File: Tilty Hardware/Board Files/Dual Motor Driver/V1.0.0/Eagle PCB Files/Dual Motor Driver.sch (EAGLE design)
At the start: 43 parts, among them J1 AVR_SPI_PRG_62X3_LOCK, Q1 16MHz, U1 ATMEGA328P, U2 L298_BRIDGE_DRIVER, U3 LM2931

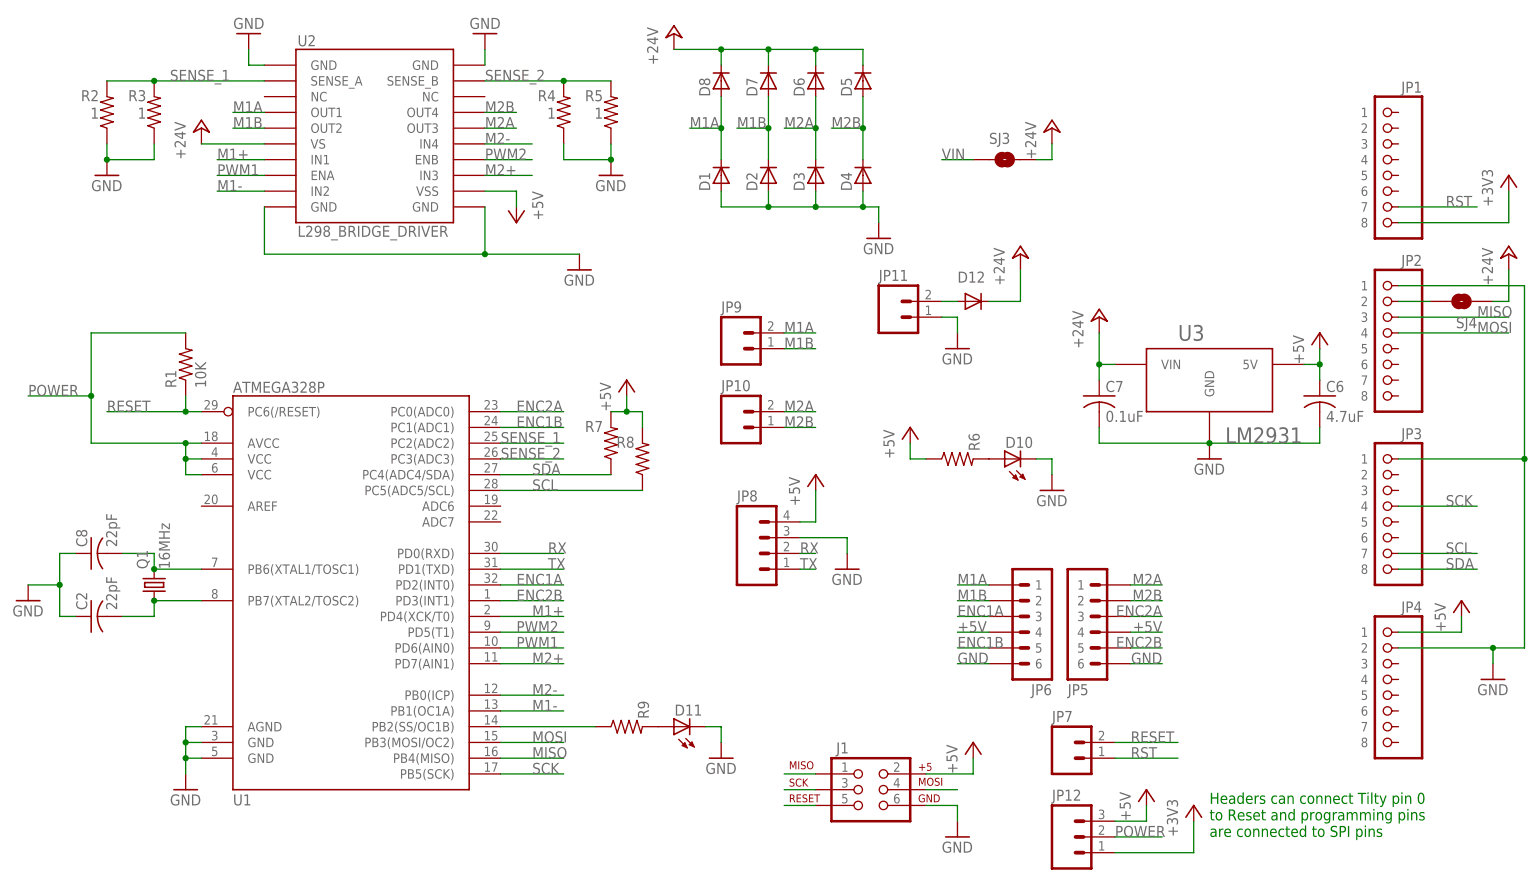
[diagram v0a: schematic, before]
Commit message: Updated some pin connection names on the Dual Motor Driver schematic
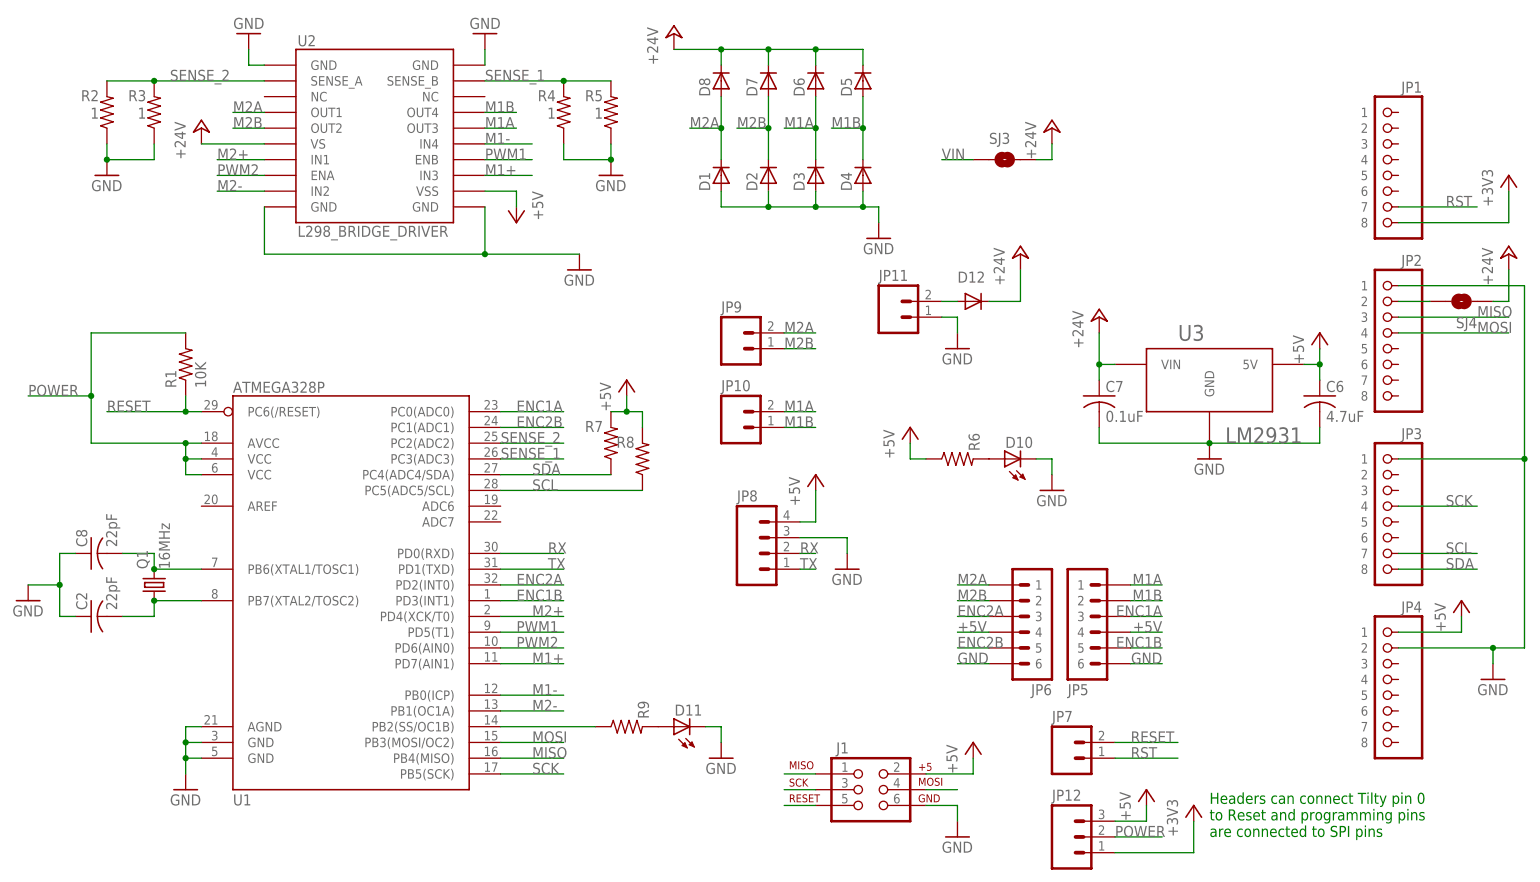
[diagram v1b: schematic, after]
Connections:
- net ENC1A: now also JP5.3, U1.PC0(ADC0); no longer JP6.3, U1.PD2(INT0)
- net ENC1B: now also JP5.5, U1.PD3(INT1); no longer JP6.5, U1.PC1(ADC1)
- net ENC2A: now also JP6.3, U1.PD2(INT0); no longer JP5.3, U1.PC0(ADC0)
- net ENC2B: now also JP6.5, U1.PC1(ADC1); no longer JP5.5, U1.PD3(INT1)
- net M1+: now also U1.PD7(AIN1), U2.IN3; no longer U1.PD4(XCK/T0), U2.IN1
- net M1-: now also U1.PB0(ICP), U2.IN4; no longer U1.PB1(OC1A), U2.IN2
- net M1A: now also D3.C, D6.A, JP10.2, JP5.1, U2.OUT3; no longer D1.C, D8.A, JP6.1, JP9.2, U2.OUT1
- net M1B: now also D4.C, D5.A, JP10.1, JP5.2, U2.OUT4; no longer D2.C, D7.A, JP6.2, JP9.1, U2.OUT2
- net M2+: now also U1.PD4(XCK/T0), U2.IN1; no longer U1.PD7(AIN1), U2.IN3
- net M2-: now also U1.PB1(OC1A), U2.IN2; no longer U1.PB0(ICP), U2.IN4
- net M2A: now also D1.C, D8.A, JP6.1, JP9.2, U2.OUT1; no longer D3.C, D6.A, JP10.2, JP5.1, U2.OUT3
- net M2B: now also D2.C, D7.A, JP6.2, JP9.1, U2.OUT2; no longer D4.C, D5.A, JP10.1, JP5.2, U2.OUT4
- net PWM1: now also U1.PD5(T1), U2.ENB; no longer U1.PD6(AIN0), U2.ENA
- net PWM2: now also U1.PD6(AIN0), U2.ENA; no longer U1.PD5(T1), U2.ENB
- net SENSE_1: now also R4.2, R5.2, U1.PC3(ADC3), U2.SENSE_B; no longer R2.2, R3.2, U1.PC2(ADC2), U2.SENSE_A
- net SENSE_2: now also R2.2, R3.2, U1.PC2(ADC2), U2.SENSE_A; no longer R4.2, R5.2, U1.PC3(ADC3), U2.SENSE_B
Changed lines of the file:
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@@
 </segment>
 </net>
-<net name="M1A" class="0">
+<net name="M2A" class="0">
 <segment>
 <pinref part="D1" gate="G$1" pin="C"/>
@@
 </segment>
 </net>
-<net name="M1B" class="0">
+<net name="M2B" class="0">
 <segment>
 <wire x1="116.84" y1="109.22" x2="116.84" y2="114.3" width="0.1524" layer="91"/>
@@
 </segment>
 </net>
-<net name="M2A" class="0">
+<net name="M1A" class="0">
 <segment>
 <wire x1="124.46" y1="109.22" x2="124.46" y2="114.3" width="0.1524" layer="91"/>
@@
 </segment>
 </net>
-<net name="M2B" class="0">
+<net name="M1B" class="0">
 <segment>
 <wire x1="132.08" y1="109.22" x2="132.08" y2="114.3" width="0.1524" layer="91"/>
@@
 </segment>
 </net>
-<net name="ENC1B" class="0">
+<net name="ENC2B" class="0">
 <segment>
 <pinref part="U1" gate="G$1" pin="PC1(ADC1)"/>
@@
 </segment>
 </net>
-<net name="ENC1A" class="0">
+<net name="ENC2A" class="0">
 <segment>
 <pinref part="JP6" gate="1" pin="3"/>
@@
 </segment>
 </net>
-<net name="ENC2B" class="0">
+<net name="ENC1B" class="0">
 <segment>
 <pinref part="U1" gate="G$1" pin="PD3(INT1)"/>
@@
 </segment>
 </net>
-<net name="ENC2A" class="0">
+<net name="ENC1A" class="0">
 <segment>
 <pinref part="U1" gate="G$1" pin="PC0(ADC0)"/>
@@
 </segment>
 </net>
-<net name="M1+" class="0">
+<net name="M2+" class="0">
 <segment>
 <pinref part="U2" gate="G$1" pin="IN1"/>
@@
 <net name="M1-" class="0">
 <segment>
-<pinref part="U2" gate="G$1" pin="IN2"/>
-<wire x1="35.56" y1="104.14" x2="27.94" y2="104.14" width="0.1524" layer="91"/>
-<label x="27.94" y="104.14" size="1.778" layer="95"/>
-</segment>
-<segment>
-<pinref part="U1" gate="G$1" pin="PB1(OC1A)"/>
-<wire x1="73.66" y1="20.32" x2="83.82" y2="20.32" width="0.1524" layer="91"/>
-<label x="78.74" y="20.32" size="1.778" layer="95"/>
-</segment>
-</net>
-<net name="M2-" class="0">
-<segment>
 <pinref part="U2" gate="G$1" pin="IN4"/>
 <wire x1="71.12" y1="111.76" x2="78.74" y2="111.76" width="0.1524" layer="91"/>
@@
 </segment>
 </net>
-<net name="M2+" class="0">
+<net name="M1+" class="0">
 <segment>
 <pinref part="U2" gate="G$1" pin="IN3"/>
@@
 </segment>
 </net>
-<net name="PWM2" class="0">
+<net name="PWM1" class="0">
 <segment>
 <pinref part="U2" gate="G$1" pin="ENB"/>
@@
 </segment>
 </net>
-<net name="PWM1" class="0">
+<net name="PWM2" class="0">
 <segment>
 <pinref part="U2" gate="G$1" pin="ENA"/>
@@
 </segment>
 </net>
-<net name="SENSE_2" class="0">
+<net name="SENSE_1" class="0">
 <segment>
 <pinref part="U2" gate="G$1" pin="SENSE_B"/>
@@
 </segment>
 </net>
-<net name="SENSE_1" class="0">
+<net name="SENSE_2" class="0">
 <segment>
 <pinref part="R2" gate="G$1" pin="2"/>
@@
 </segment>
 </net>
+<net name="M2-" class="0">
+<segment>
+<pinref part="U1" gate="G$1" pin="PB1(OC1A)"/>
+<wire x1="73.66" y1="20.32" x2="83.82" y2="20.32" width="0.1524" layer="91"/>
+<label x="78.74" y="20.32" size="1.778" layer="95"/>
+</segment>
+<segment>
+<pinref part="U2" gate="G$1" pin="IN2"/>
+<wire x1="35.56" y1="104.14" x2="27.94" y2="104.14" width="0.1524" layer="91"/>
+<label x="27.94" y="104.14" size="1.778" layer="95"/>
+</segment>
+</net>
